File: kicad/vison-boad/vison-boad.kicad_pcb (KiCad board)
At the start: 2 copper layers, 80 x 100 mm, 29 parts, among them J1 USB_C_Receptacle_USB2.0, J2 Wio Terminal, J3 UART, J4 pin_test, J5 NEO PIXEL, J6 to main, J7 I2C_0, SW1 BOOTSET, SW2 RESET, SW3 M1n_RST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

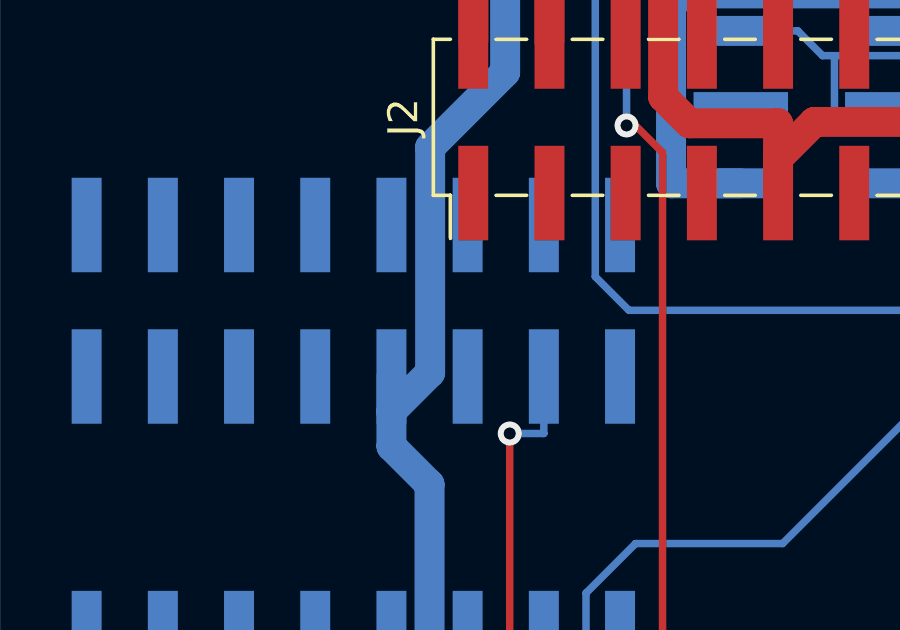
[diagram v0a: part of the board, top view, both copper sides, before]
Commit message: Modify Wio coneector
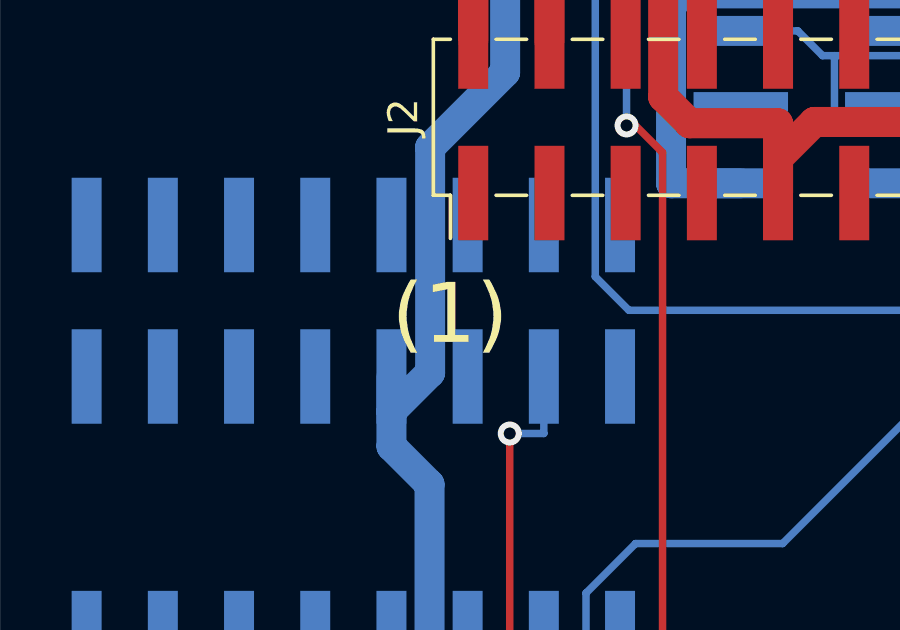
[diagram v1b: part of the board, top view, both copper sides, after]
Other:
- board text added: "(1)"
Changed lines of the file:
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@@
     (fp_arc (start 11.1379 -1.270002) (mid 10.765926 -0.371975) (end 9.8679 -0.000002) (layer "B.SilkS") (width 0.2))
     (fp_arc (start -9.8679 -0.000002) (mid -10.765926 -0.371976) (end -11.1379 -1.270002) (layer "B.SilkS") (width 0.2))
-    (fp_arc (start 0.59659 -31.775402) (mid 1.11314 -31.672653) (end 1.551051 -31.380051) (layer "B.SilkS") (width 0.2))
+    (fp_arc (start 0.59659 -31.775402) (mid 1.113141 -31.672654) (end 1.551051 -31.380051) (layer "B.SilkS") (width 0.2))
     (fp_arc (start -11.1379 -29.768802) (mid -10.765926 -30.666828) (end -9.8679 -31.038802) (layer "B.SilkS") (width 0.2))
     (fp_circle (center 8.8773 -29.819602) (end 8.4074 -29.819602) (layer "B.SilkS") (width 0.2) (fill none))
@@
     (fp_arc (start -11.1379 -29.768802) (mid -10.765926 -30.666828) (end -9.8679 -31.038802) (layer "B.SilkS") (width 0.2))
     (fp_arc (start -9.8679 -0.000002) (mid -10.765926 -0.371976) (end -11.1379 -1.270002) (layer "B.SilkS") (width 0.2))
-    (fp_arc (start 0.59659 -31.775402) (mid 1.11314 -31.672653) (end 1.551051 -31.380051) (layer "B.SilkS") (width 0.2))
+    (fp_arc (start 0.59659 -31.775402) (mid 1.113141 -31.672654) (end 1.551051 -31.380051) (layer "B.SilkS") (width 0.2))
     (fp_arc (start 11.1379 -1.270002) (mid 10.765926 -0.371975) (end 9.8679 -0.000002) (layer "B.SilkS") (width 0.2))
     (fp_circle (center 8.8773 -29.819602) (end 8.4074 -29.819602) (layer "B.SilkS") (width 0.2) (fill none))
@@
     (fp_arc (start 2.3749 -31.038802) (mid 1.929036 -31.12749) (end 1.551051 -31.380051) (layer "B.SilkS") (width 0.2))
     (fp_arc (start -2.130146 -31.380051) (mid -1.692236 -31.672654) (end -1.175685 -31.775402) (layer "B.SilkS") (width 0.2))
-    (fp_arc (start 0.59659 -31.775402) (mid 1.11314 -31.672653) (end 1.551051 -31.380051) (layer "B.SilkS") (width 0.2))
+    (fp_arc (start 0.59659 -31.775402) (mid 1.113141 -31.672654) (end 1.551051 -31.380051) (layer "B.SilkS") (width 0.2))
     (fp_arc (start -2.130146 -31.380051) (mid -2.508131 -31.12749) (end -2.953995 -31.038802) (layer "B.SilkS") (width 0.2))
     (fp_arc (start -9.8679 -0.000002) (mid -10.765926 -0.371976) (end -11.1379 -1.270002) (layer "B.SilkS") (width 0.2))
@@
     (fp_line (start -2.95 -8.1) (end -1.93 -8.1) (layer "B.SilkS") (width 0.12))
     (fp_line (start -1.857299 -9.610603) (end -1.857299 -7.407401) (layer "B.SilkS") (width 0.2))
-    (fp_arc (start 0.59659 -31.775402) (mid 1.11314 -31.672653) (end 1.551051 -31.380051) (layer "B.SilkS") (width 0.2))
+    (fp_arc (start 0.59659 -31.775402) (mid 1.113141 -31.672654) (end 1.551051 -31.380051) (layer "B.SilkS") (width 0.2))
     (fp_arc (start -2.130146 -31.380051) (mid -2.508131 -31.12749) (end -2.953995 -31.038802) (layer "B.SilkS") (width 0.2))
     (fp_arc (start 11.1379 -1.270002) (mid 10.765926 -0.371975) (end 9.8679 -0.000002) (layer "B.SilkS") (width 0.2))
@@
     (fp_arc (start -2.130146 -31.380051) (mid -2.508131 -31.12749) (end -2.953995 -31.038802) (layer "B.SilkS") (width 0.2))
     (fp_arc (start -9.8679 -0.000002) (mid -10.765926 -0.371976) (end -11.1379 -1.270002) (layer "B.SilkS") (width 0.2))
-    (fp_arc (start 0.59659 -31.775402) (mid 1.11314 -31.672653) (end 1.551051 -31.380051) (layer "B.SilkS") (width 0.2))
+    (fp_arc (start 0.59659 -31.775402) (mid 1.113141 -31.672654) (end 1.551051 -31.380051) (layer "B.SilkS") (width 0.2))
     (fp_arc (start 2.3749 -31.038802) (mid 1.929036 -31.12749) (end 1.551051 -31.380051) (layer "B.SilkS") (width 0.2))
     (fp_arc (start 9.8679 -31.038802) (mid 10.765926 -30.666828) (end 11.1379 -29.768802) (layer "B.SilkS") (width 0.2))
@@
   (gr_arc (start 190 134.171573) (mid 189.847768 134.936945) (end 189.414214 135.585786) (layer "Edge.Cuts") (width 0.2))
   (gr_arc (start 110 65.828427) (mid 110.152241 65.06306) (end 110.585786 64.414214) (layer "Edge.Cuts") (width 0.2))
+  (gr_text "(1)" (at 125.095 99.06) (layer "F.SilkS")
+    (effects (font (size 2 2) (thickness 0.3)))
+  )
   (segment (start 141.566 132.634) (end 138.25 135.95) (width 0.25) (layer "F.Cu") (net 1))
   (segment (start 147.02 71.65) (end 147.02 63.6843) (width 0.25) (layer "F.Cu") (net 1))

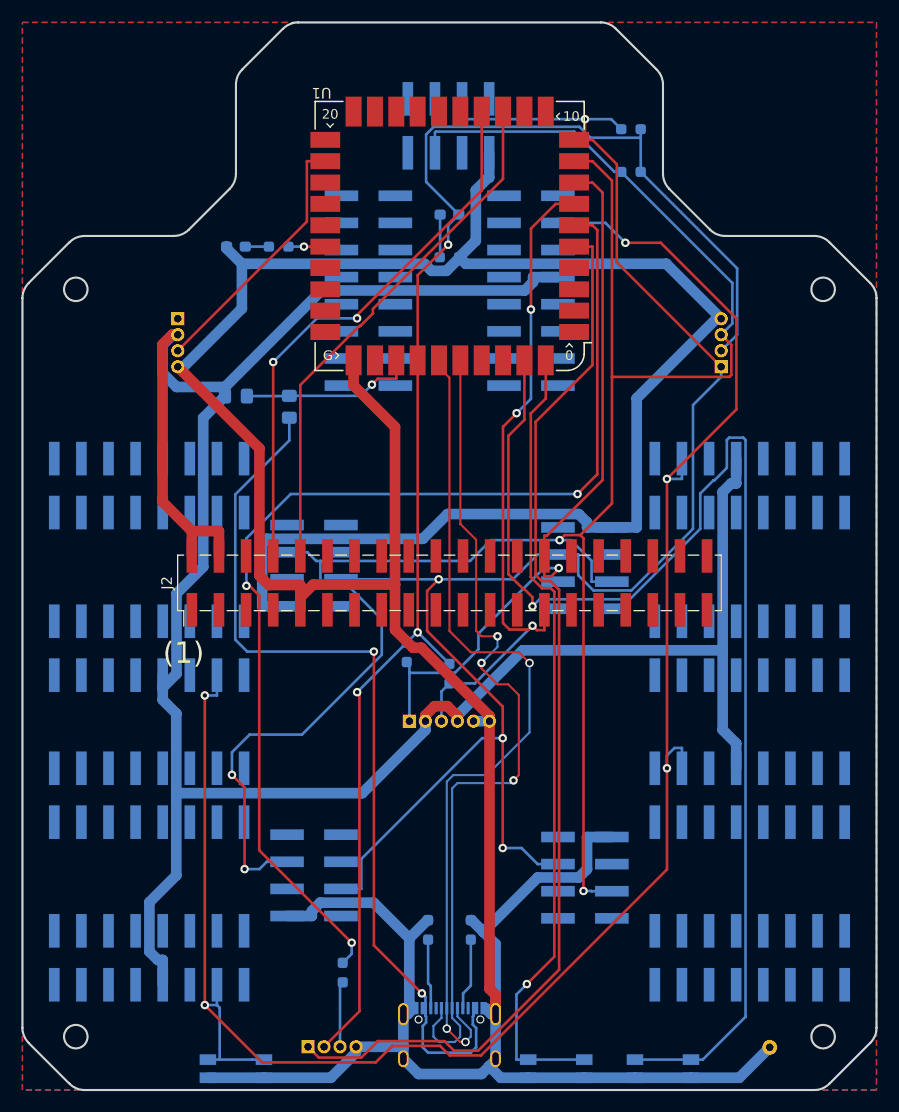
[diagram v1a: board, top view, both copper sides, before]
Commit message: fix: vison-board GND
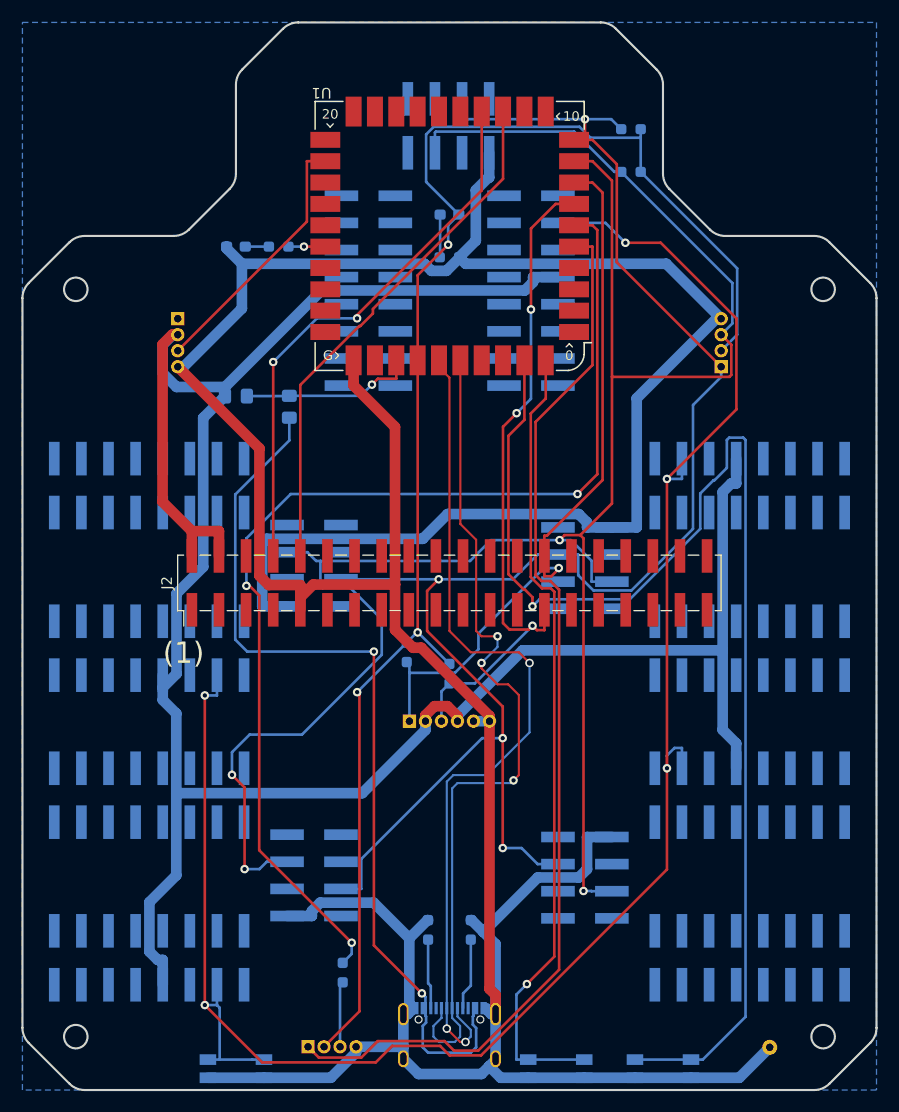
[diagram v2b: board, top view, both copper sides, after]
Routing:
- removed copper zone on F.Cu, net GND
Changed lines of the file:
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@@
     (fp_arc (start 11.1379 -1.270002) (mid 10.765926 -0.371975) (end 9.8679 -0.000002) (layer "B.SilkS") (width 0.2))
     (fp_arc (start -9.8679 -0.000002) (mid -10.765926 -0.371976) (end -11.1379 -1.270002) (layer "B.SilkS") (width 0.2))
-    (fp_arc (start 0.59659 -31.775402) (mid 1.113141 -31.672654) (end 1.551051 -31.380051) (layer "B.SilkS") (width 0.2))
+    (fp_arc (start 0.59659 -31.775402) (mid 1.11314 -31.672653) (end 1.551051 -31.380051) (layer "B.SilkS") (width 0.2))
     (fp_arc (start -11.1379 -29.768802) (mid -10.765926 -30.666828) (end -9.8679 -31.038802) (layer "B.SilkS") (width 0.2))
     (fp_circle (center 8.8773 -29.819602) (end 8.4074 -29.819602) (layer "B.SilkS") (width 0.2) (fill none))
@@
     (fp_arc (start -11.1379 -29.768802) (mid -10.765926 -30.666828) (end -9.8679 -31.038802) (layer "B.SilkS") (width 0.2))
     (fp_arc (start -9.8679 -0.000002) (mid -10.765926 -0.371976) (end -11.1379 -1.270002) (layer "B.SilkS") (width 0.2))
-    (fp_arc (start 0.59659 -31.775402) (mid 1.113141 -31.672654) (end 1.551051 -31.380051) (layer "B.SilkS") (width 0.2))
+    (fp_arc (start 0.59659 -31.775402) (mid 1.11314 -31.672653) (end 1.551051 -31.380051) (layer "B.SilkS") (width 0.2))
     (fp_arc (start 11.1379 -1.270002) (mid 10.765926 -0.371975) (end 9.8679 -0.000002) (layer "B.SilkS") (width 0.2))
     (fp_circle (center 8.8773 -29.819602) (end 8.4074 -29.819602) (layer "B.SilkS") (width 0.2) (fill none))
@@
     (fp_arc (start 2.3749 -31.038802) (mid 1.929036 -31.12749) (end 1.551051 -31.380051) (layer "B.SilkS") (width 0.2))
     (fp_arc (start -2.130146 -31.380051) (mid -1.692236 -31.672654) (end -1.175685 -31.775402) (layer "B.SilkS") (width 0.2))
-    (fp_arc (start 0.59659 -31.775402) (mid 1.113141 -31.672654) (end 1.551051 -31.380051) (layer "B.SilkS") (width 0.2))
+    (fp_arc (start 0.59659 -31.775402) (mid 1.11314 -31.672653) (end 1.551051 -31.380051) (layer "B.SilkS") (width 0.2))
     (fp_arc (start -2.130146 -31.380051) (mid -2.508131 -31.12749) (end -2.953995 -31.038802) (layer "B.SilkS") (width 0.2))
     (fp_arc (start -9.8679 -0.000002) (mid -10.765926 -0.371976) (end -11.1379 -1.270002) (layer "B.SilkS") (width 0.2))
@@
     (fp_line (start -2.95 -8.1) (end -1.93 -8.1) (layer "B.SilkS") (width 0.12))
     (fp_line (start -1.857299 -9.610603) (end -1.857299 -7.407401) (layer "B.SilkS") (width 0.2))
-    (fp_arc (start 0.59659 -31.775402) (mid 1.113141 -31.672654) (end 1.551051 -31.380051) (layer "B.SilkS") (width 0.2))
+    (fp_arc (start 0.59659 -31.775402) (mid 1.11314 -31.672653) (end 1.551051 -31.380051) (layer "B.SilkS") (width 0.2))
     (fp_arc (start -2.130146 -31.380051) (mid -2.508131 -31.12749) (end -2.953995 -31.038802) (layer "B.SilkS") (width 0.2))
     (fp_arc (start 11.1379 -1.270002) (mid 10.765926 -0.371975) (end 9.8679 -0.000002) (layer "B.SilkS") (width 0.2))
@@
     (fp_arc (start -2.130146 -31.380051) (mid -2.508131 -31.12749) (end -2.953995 -31.038802) (layer "B.SilkS") (width 0.2))
     (fp_arc (start -9.8679 -0.000002) (mid -10.765926 -0.371976) (end -11.1379 -1.270002) (layer "B.SilkS") (width 0.2))
-    (fp_arc (start 0.59659 -31.775402) (mid 1.113141 -31.672654) (end 1.551051 -31.380051) (layer "B.SilkS") (width 0.2))
+    (fp_arc (start 0.59659 -31.775402) (mid 1.11314 -31.672653) (end 1.551051 -31.380051) (layer "B.SilkS") (width 0.2))
     (fp_arc (start 2.3749 -31.038802) (mid 1.929036 -31.12749) (end 1.551051 -31.380051) (layer "B.SilkS") (width 0.2))
     (fp_arc (start 9.8679 -31.038802) (mid 10.765926 -30.666828) (end 11.1379 -29.768802) (layer "B.SilkS") (width 0.2))
@@
   (segment (start 140.7252 92.9852) (end 143.6572 95.9172) (width 0.25) (layer "B.Cu") (net 259))
   (segment (start 153.8809 88.4924) (end 151.9282 90.4451) (width 0.25) (layer "B.Cu") (net 259))
-  (zone (net 6) (net_name "GND") (layers F&B.Cu) (hatch edge 0.508)
+  (zone (net 6) (net_name "GND") (layer "B.Cu") (hatch edge 0.508)
     (connect_pads (clearance 0.508))
     (min_thickness 0.254) (filled_areas_thickness no)

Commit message: MMA LOGO
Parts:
- added G***: LOGO, 0.main.robot:MMA_Logo, F.Cu at (181.0, 76.8)
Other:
- board text added: "Mar.2023 A.Saeki"

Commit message: fix: main
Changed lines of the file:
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@@
     (fp_line (start -1 0.3) (end -1 -0.6) (layer "B.Fab") (width 0.1))
     (fp_line (start -0.7 0.6) (end -1 0.3) (layer "B.Fab") (width 0.1))
-    (pad "1" smd roundrect (at -1.025 0 270) (size 1.15 1.4) (layers "B.Cu" "B.Paste" "B.Mask") (roundrect_rratio 0.217391)
+    (pad "1" smd roundrect (at -1.025 0 270) (size 1.15 1.4) (layers "B.Cu" "B.Paste" "B.Mask") (roundrect_rratio 0.2173913043)
       (net 19 "Net-(D1-Pad1)") (pinfunction "K") (pintype "passive"))
-    (pad "2" smd roundrect (at 1.025 0 270) (size 1.15 1.4) (layers "B.Cu" "B.Paste" "B.Mask") (roundrect_rratio 0.217391)
+    (pad "2" smd roundrect (at 1.025 0 270) (size 1.15 1.4) (layers "B.Cu" "B.Paste" "B.Mask") (roundrect_rratio 0.2173913043)
       (net 20 "VBUS") (pinfunction "A") (pintype "passive"))
     (model "${KICAD6_3DMODEL_DIR}/Diode_SMD.3dshapes/D_0805_2012Metric.wrl"
@@
     (fp_arc (start 11.1379 -1.270002) (mid 10.765926 -0.371975) (end 9.8679 -0.000002) (layer "B.SilkS") (width 0.2))
     (fp_arc (start -9.8679 -0.000002) (mid -10.765926 -0.371976) (end -11.1379 -1.270002) (layer "B.SilkS") (width 0.2))
-    (fp_arc (start 0.59659 -31.775402) (mid 1.113141 -31.672654) (end 1.551051 -31.380051) (layer "B.SilkS") (width 0.2))
+    (fp_arc (start 0.59659 -31.775402) (mid 1.11314 -31.672653) (end 1.551051 -31.380051) (layer "B.SilkS") (width 0.2))
     (fp_arc (start -11.1379 -29.768802) (mid -10.765926 -30.666828) (end -9.8679 -31.038802) (layer "B.SilkS") (width 0.2))
     (fp_circle (center 8.8773 -29.819602) (end 8.4074 -29.819602) (layer "B.SilkS") (width 0.2) (fill none))
@@
     (fp_line (start -0.7 0.6) (end -1 0.3) (layer "B.Fab") (width 0.1))
     (fp_line (start 1 -0.6) (end 1 0.6) (layer "B.Fab") (width 0.1))
-    (pad "1" smd roundrect (at -1.025 0 180) (size 1.15 1.4) (layers "B.Cu" "B.Paste" "B.Mask") (roundrect_rratio 0.217391)
+    (pad "1" smd roundrect (at -1.025 0 180) (size 1.15 1.4) (layers "B.Cu" "B.Paste" "B.Mask") (roundrect_rratio 0.2173913043)
       (net 19 "Net-(D1-Pad1)") (pinfunction "K") (pintype "passive"))
-    (pad "2" smd roundrect (at 1.025 0 180) (size 1.15 1.4) (layers "B.Cu" "B.Paste" "B.Mask") (roundrect_rratio 0.217391)
+    (pad "2" smd roundrect (at 1.025 0 180) (size 1.15 1.4) (layers "B.Cu" "B.Paste" "B.Mask") (roundrect_rratio 0.2173913043)
       (net 21 "+5V") (pinfunction "A") (pintype "passive"))
     (model "${KICAD6_3DMODEL_DIR}/Diode_SMD.3dshapes/D_0805_2012Metric.wrl"
@@
     (fp_arc (start -11.1379 -29.768802) (mid -10.765926 -30.666828) (end -9.8679 -31.038802) (layer "B.SilkS") (width 0.2))
     (fp_arc (start -9.8679 -0.000002) (mid -10.765926 -0.371976) (end -11.1379 -1.270002) (layer "B.SilkS") (width 0.2))
-    (fp_arc (start 0.59659 -31.775402) (mid 1.113141 -31.672654) (end 1.551051 -31.380051) (layer "B.SilkS") (width 0.2))
+    (fp_arc (start 0.59659 -31.775402) (mid 1.11314 -31.672653) (end 1.551051 -31.380051) (layer "B.SilkS") (width 0.2))
     (fp_arc (start 11.1379 -1.270002) (mid 10.765926 -0.371975) (end 9.8679 -0.000002) (layer "B.SilkS") (width 0.2))
     (fp_circle (center 8.8773 -29.819602) (end 8.4074 -29.819602) (layer "B.SilkS") (width 0.2) (fill none))
@@
     (fp_arc (start 2.3749 -31.038802) (mid 1.929036 -31.12749) (end 1.551051 -31.380051) (layer "B.SilkS") (width 0.2))
     (fp_arc (start -2.130146 -31.380051) (mid -1.692236 -31.672654) (end -1.175685 -31.775402) (layer "B.SilkS") (width 0.2))
-    (fp_arc (start 0.59659 -31.775402) (mid 1.113141 -31.672654) (end 1.551051 -31.380051) (layer "B.SilkS") (width 0.2))
+    (fp_arc (start 0.59659 -31.775402) (mid 1.11314 -31.672653) (end 1.551051 -31.380051) (layer "B.SilkS") (width 0.2))
     (fp_arc (start -2.130146 -31.380051) (mid -2.508131 -31.12749) (end -2.953995 -31.038802) (layer "B.SilkS") (width 0.2))
     (fp_arc (start -9.8679 -0.000002) (mid -10.765926 -0.371976) (end -11.1379 -1.270002) (layer "B.SilkS") (width 0.2))
@@
     (fp_line (start -2.95 -8.1) (end -1.93 -8.1) (layer "B.SilkS") (width 0.12))
     (fp_line (start -1.857299 -9.610603) (end -1.857299 -7.407401) (layer "B.SilkS") (width 0.2))
-    (fp_arc (start 0.59659 -31.775402) (mid 1.113141 -31.672654) (end 1.551051 -31.380051) (layer "B.SilkS") (width 0.2))
+    (fp_arc (start 0.59659 -31.775402) (mid 1.11314 -31.672653) (end 1.551051 -31.380051) (layer "B.SilkS") (width 0.2))
     (fp_arc (start -2.130146 -31.380051) (mid -2.508131 -31.12749) (end -2.953995 -31.038802) (layer "B.SilkS") (width 0.2))
     (fp_arc (start 11.1379 -1.270002) (mid 10.765926 -0.371975) (end 9.8679 -0.000002) (layer "B.SilkS") (width 0.2))
@@
     (fp_arc (start -2.130146 -31.380051) (mid -2.508131 -31.12749) (end -2.953995 -31.038802) (layer "B.SilkS") (width 0.2))
     (fp_arc (start -9.8679 -0.000002) (mid -10.765926 -0.371976) (end -11.1379 -1.270002) (layer "B.SilkS") (width 0.2))
-    (fp_arc (start 0.59659 -31.775402) (mid 1.113141 -31.672654) (end 1.551051 -31.380051) (layer "B.SilkS") (width 0.2))
+    (fp_arc (start 0.59659 -31.775402) (mid 1.11314 -31.672653) (end 1.551051 -31.380051) (layer "B.SilkS") (width 0.2))
     (fp_arc (start 2.3749 -31.038802) (mid 1.929036 -31.12749) (end 1.551051 -31.380051) (layer "B.SilkS") (width 0.2))
     (fp_arc (start 9.8679 -31.038802) (mid 10.765926 -30.666828) (end 11.1379 -29.768802) (layer "B.SilkS") (width 0.2))
